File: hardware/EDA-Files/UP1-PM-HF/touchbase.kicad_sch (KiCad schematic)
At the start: 12 parts, among them J10 LD2420 / TOFx, J20 VEML7700, J30 I2C Sensor Extension, J40 Extension, Q1 2N7002

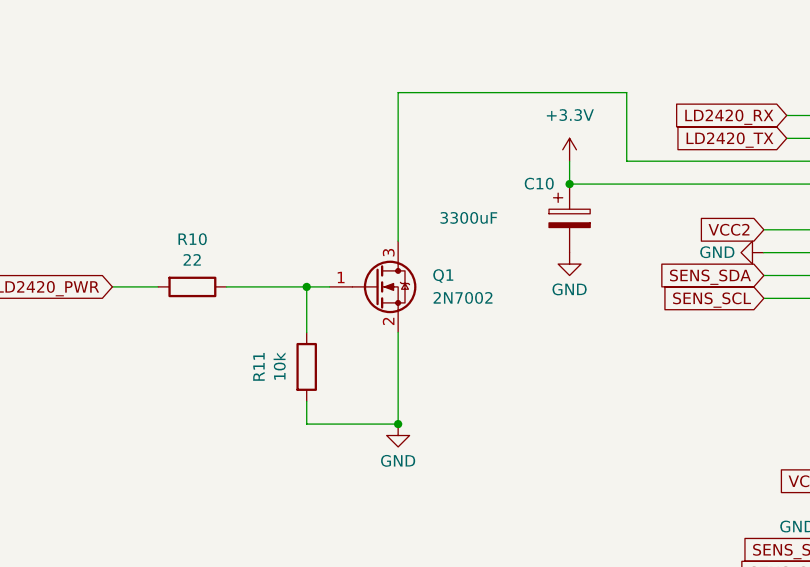
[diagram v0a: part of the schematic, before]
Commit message: UP1-PM-HF V00.20: - add reset IC
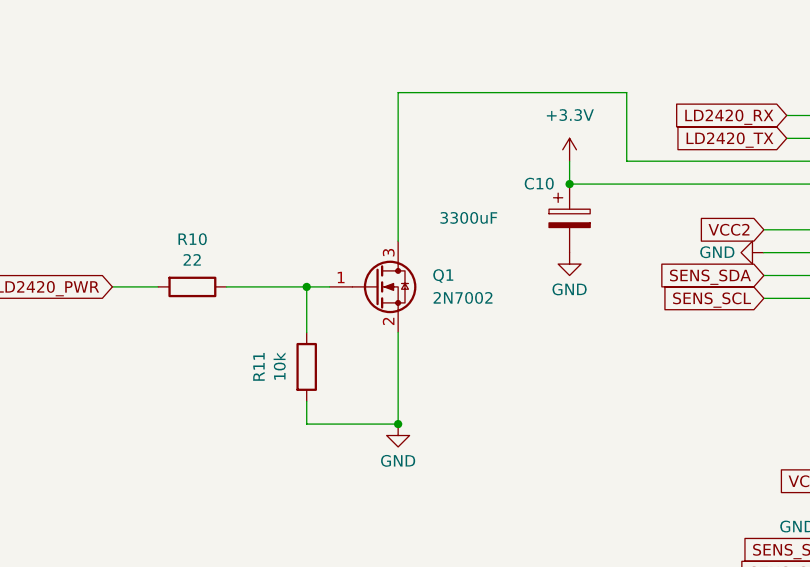
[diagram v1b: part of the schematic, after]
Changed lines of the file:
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@@
 (kicad_sch
-	(version 20231120)
+	(version 20250114)
 	(generator "eeschema")
-	(generator_version "8.0")
+	(generator_version "9.0")
 	(paper "A4")
 	(title_block
 		(title "UP1-PM-HF")
-		(date "2025-02-05")
-		(rev "V00.10")
+		(date "2025-12-09")
+		(rev "V00.20")
 		(company "OpenKNX")
 		(comment 1 "by Ing-Dom <dom@ing-dom.de>")
@@
 			)
 		)
-		(property "Description" ""
-			(at 144.78 100.33 0)
-			(effects
-				(font
-					(size 1.27 1.27)
-				)
-				(hide yes)
-			)
-		)
-		(property "PartNo" ""
+		(property "Description" "Unpolarized capacitor"
 			(at 144.78 100.33 0)
 			(effects
@@
 			)
 		)
-		(property "PartNo" ""
-			(at 59.69 50.8 0)
-			(effects
-				(font
-					(size 1.27 1.27)
-				)
-				(hide yes)
-			)
-		)
 		(pin "2"
 		)
@@
 			)
 		)
-		(property "Description" ""
-			(at 144.78 30.48 0)
-			(effects
-				(font
-					(size 1.27 1.27)
-				)
-				(hide yes)
-			)
-		)
-		(property "PartNo" ""
+		(property "Description" "Unpolarized capacitor"
 			(at 144.78 30.48 0)
 			(effects
@@
 			)
 		)
-		(property "PartNo" ""
-			(at 125.73 77.47 0)
-			(effects
-				(font
-					(size 1.27 1.27)
-				)
-				(hide yes)
-			)
-		)
 		(pin "3"
 		)
@@
 			)
 		)
-		(property "Description" ""
-			(at 144.78 54.61 0)
-			(effects
-				(font
-					(size 1.27 1.27)
-				)
-				(hide yes)
-			)
-		)
-		(property "PartNo" ""
+		(property "Description" "Unpolarized capacitor"
 			(at 144.78 54.61 0)
 			(effects
@@
 			)
 		)
-		(property "Description" ""
-			(at 39.37 50.8 0)
-			(effects
-				(font
-					(size 1.27 1.27)
-				)
-				(hide yes)
-			)
-		)
-		(property "PartNo" ""
+		(property "Description" "Resistor"
 			(at 39.37 50.8 0)
 			(effects
@@
 			)
 		)
-		(property "Description" ""
-			(at 52.07 59.69 0)
-			(effects
-				(font
-					(size 1.27 1.27)
-				)
-				(hide yes)
-			)
-		)
-		(property "PartNo" ""
+		(property "Description" "Resistor"
 			(at 52.07 59.69 0)
 			(effects
@@
 			)
 		)
-		(property "PartNo" ""
-			(at 81.28 43.18 0)
-			(effects
-				(font
-					(size 1.27 1.27)
-				)
-				(hide yes)
-			)
-		)
 		(pin "2"
 		)
@@
 			)
 		)
-		(property "PartNo" ""
-			(at 121.92 125.73 0)
-			(effects
-				(font
-					(size 1.27 1.27)
-				)
-				(hide yes)
-			)
-		)
 		(pin "2"
 		)
@@
 			)
 		)
-		(property "PartNo" ""
-			(at 123.19 43.18 0)
-			(effects
-				(font
-					(size 1.27 1.27)
-				)
-				(hide yes)
-			)
-		)
 		(pin "3"
 		)
@@
 			)
 		)
-		(property "Description" ""
-			(at 144.78 77.47 0)
-			(effects
-				(font
-					(size 1.27 1.27)
-				)
-				(hide yes)
-			)
-		)
-		(property "PartNo" ""
+		(property "Description" "Unpolarized capacitor"
 			(at 144.78 77.47 0)
 			(effects
@@
 			)
 		)
-		(property "Description" ""
+		(property "Description" "Generic connector, single row, 01x04, script generated (kicad-library-utils/schlib/autogen/connector/)"
 			(at 120.65 99.06 0)
 			(effects
-				(font
-					(size 1.27 1.27)
-				)
-				(hide yes)
-			)
-		)
-		(property "PartNo" ""
-			(at 120.65 99.06 0)
-			(effects

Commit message: UP1-PM-HF V00.21 * variable Flash (W25Q) * move FP to OpenKNX KiCAD Lib * increase Pad size for hand solder pins * change RP2040 reset circuit
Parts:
- C10: footprint DomsKiCADLib:CP_Radial_D10.0mm_H20.0mm_P5.00mm_Horizontal -> OpenKNX:CP_Radial_D10.0mm_H20.0mm_P5.00mm_Horizontal
- J10: footprint DomsKiCADLib:HLK_TOF_reverse_mount -> OpenKNX:HLK_TOF_reverse_mount
- J20: footprint DomsKiCADLib:VEML7700_reverse_mount -> OpenKNX:VEML7700_reverse_mount
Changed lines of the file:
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@@
 	(title_block
 		(title "UP1-PM-HF")
-		(date "2025-12-09")
-		(rev "V00.20")
+		(date "2026-02-06")
+		(rev "V00.21")
 		(company "OpenKNX")
 		(comment 1 "by Ing-Dom <dom@ing-dom.de>")
@@
 			)
 		)
-		(property "Footprint" "DomsKiCADLib:VEML7700_reverse_mount"
+		(property "Footprint" "OpenKNX:VEML7700_reverse_mount"
 			(at 125.73 77.47 0)
 			(effects
@@
 			)
 		)
-		(property "Footprint" "DomsKiCADLib:CP_Radial_D10.0mm_H20.0mm_P5.00mm_Horizontal"
+		(property "Footprint" "OpenKNX:CP_Radial_D10.0mm_H20.0mm_P5.00mm_Horizontal"
 			(at 82.2452 46.99 0)
 			(effects
@@
 			)
 		)
-		(property "Footprint" "DomsKiCADLib:HLK_TOF_reverse_mount"
+		(property "Footprint" "OpenKNX:HLK_TOF_reverse_mount"
 			(at 123.19 43.18 0)
 			(effects
